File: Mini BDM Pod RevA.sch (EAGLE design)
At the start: 37 parts

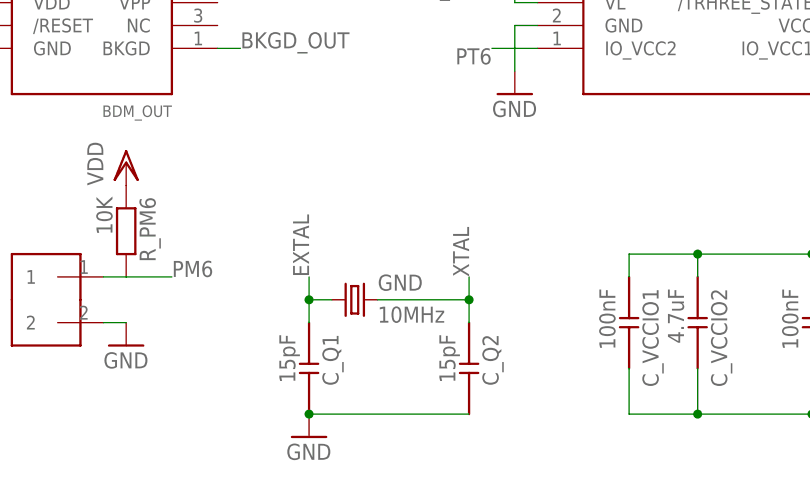
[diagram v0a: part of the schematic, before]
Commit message: prepared mounting diagram
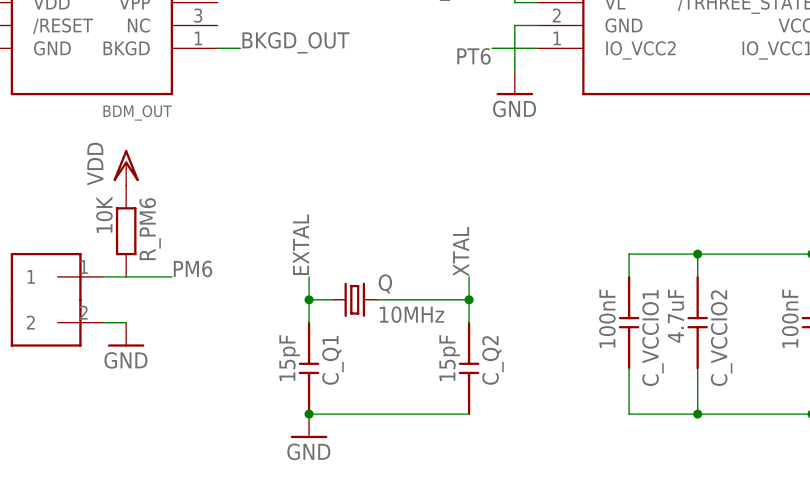
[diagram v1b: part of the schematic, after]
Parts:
- renumbered GND to Q
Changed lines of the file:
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@@
 <?xml version="1.0" encoding="utf-8"?>
 <!DOCTYPE eagle SYSTEM "eagle.dtd">
-<eagle version="6.1">
+<eagle version="6.0">
 <drawing>
 <settings>
@@
 <part name="BDM_OUT" library="myLibrary" deviceset="BDM" device=""/>
 <part name="JUMPER" library="myLibrary" deviceset="1X2" device=""/>
-<part name="GND" library="crystal" deviceset="CRYSTAL" device="HC49U70" value="10MHz"/>
+<part name="Q" library="crystal" deviceset="CRYSTAL" device="HC49U70" value="10MHz"/>
 <part name="VDD1" library="supply1" deviceset="VDD" device=""/>
 <part name="VDD2" library="supply1" deviceset="VDD" device=""/>
@@
 <instance part="BDM_OUT" gate="G$1" x="35.56" y="50.8" rot="R180"/>
 <instance part="JUMPER" gate="G$1" x="30.48" y="20.32" rot="R270"/>
-<instance part="GND" gate="G$1" x="63.5" y="20.32"/>
+<instance part="Q" gate="G$1" x="63.5" y="20.32"/>
 <instance part="VDD1" gate="G$1" x="40.64" y="157.48"/>
 <instance part="VDD2" gate="G$1" x="17.78" y="86.36"/>
@@
 <wire x1="58.42" y1="17.78" x2="58.42" y2="20.32" width="0.1524" layer="91"/>
 <label x="58.42" y="22.86" size="1.778" layer="95" rot="R90"/>
-<pinref part="GND" gate="G$1" pin="1"/>
+<pinref part="Q" gate="G$1" pin="1"/>
 <wire x1="58.42" y1="20.32" x2="58.42" y2="22.86" width="0.1524" layer="91"/>
 <wire x1="60.96" y1="20.32" x2="58.42" y2="20.32" width="0.1524" layer="91"/>
@@
 <wire x1="76.2" y1="17.78" x2="76.2" y2="20.32" width="0.1524" layer="91"/>
 <label x="76.2" y="22.86" size="1.778" layer="95" rot="R90"/>
-<pinref part="GND" gate="G$1" pin="2"/>
+<pinref part="Q" gate="G$1" pin="2"/>
 <wire x1="76.2" y1="20.32" x2="76.2" y2="22.86" width="0.1524" layer="91"/>
 <wire x1="66.04" y1="20.32" x2="76.2" y2="20.32" width="0.1524" layer="91"/>
